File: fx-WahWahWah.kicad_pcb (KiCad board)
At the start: 2 copper layers, 58.4 x 76.2 mm, 37 parts, among them J1 Conn_01x10, Q1 2N5088, Q2 2N5089

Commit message: Fix readme, add OSHW silks
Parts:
- added QR*****: fx-WahWahWah-repo, QRCodes:fx-WahWahWah-repo, F.Cu at (96.1, 89.8)
- added REF**: OSHW-Symbol_8.9x8mm_SilkScreen, Symbol:OSHW-Symbol_8.9x8mm_SilkScreen, F.Cu at (96.1, 79.8)
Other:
- board text added: "CERN-OHL-P"

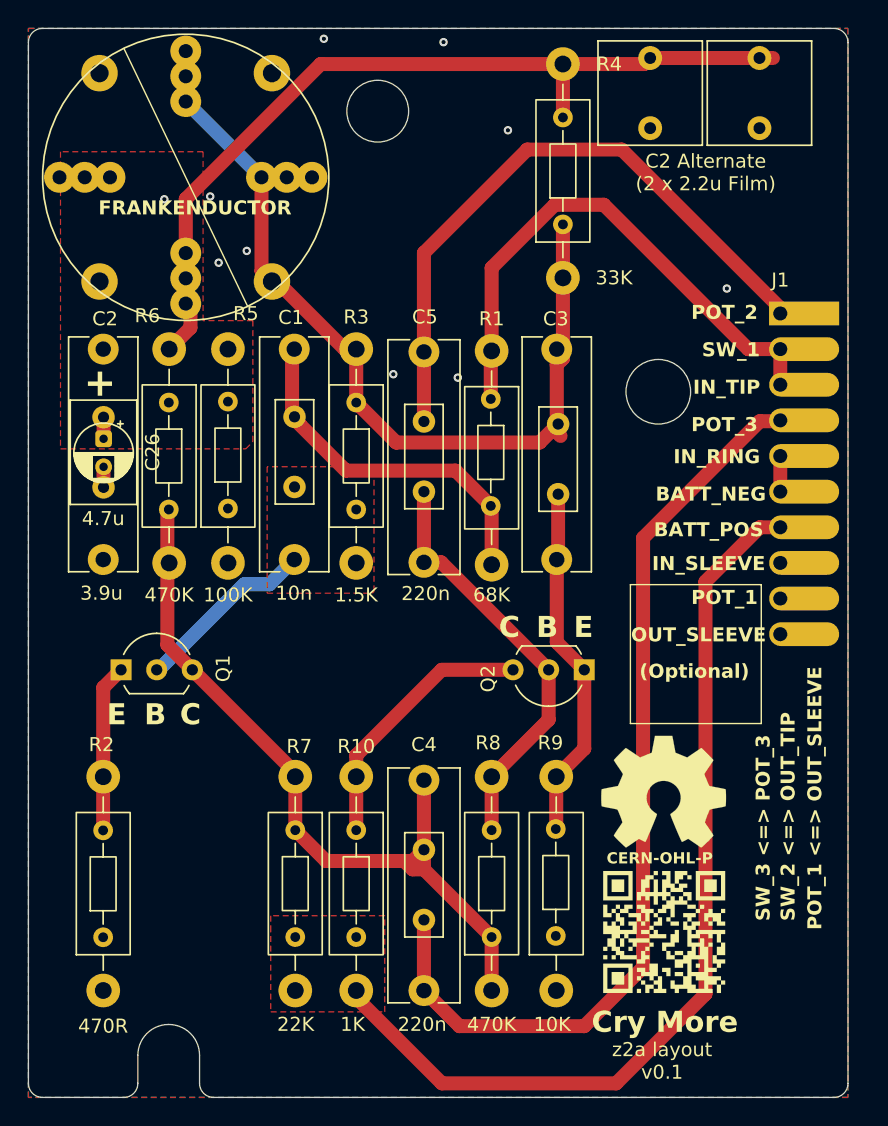
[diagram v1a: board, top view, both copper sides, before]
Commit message: Fix silks for OSHW/repo pointer
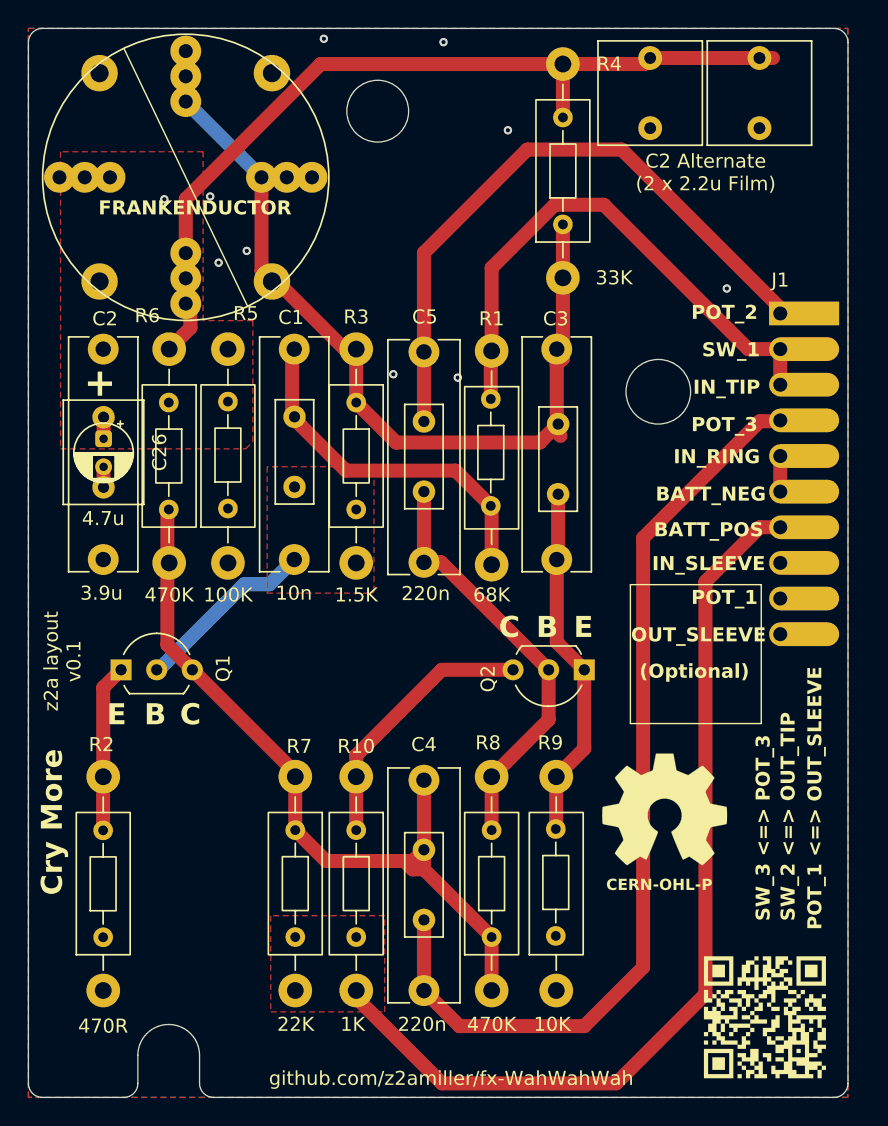
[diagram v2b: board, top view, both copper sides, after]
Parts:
- C26: footprint Capacitor_THT:C_Rect_L7.2mm_W4.5mm_P5.00mm_FKS2_FKP2_MKS2_MKP2 -> Capacitor_THT:C_Rect_L7.2mm_W5.5mm_P5.00mm_FKS2_FKP2_MKS2_MKP2
- moved QR***** 9.41 mm to (103.3, 95.9)
- moved REF** 1.26 mm to (96.1, 81.1)
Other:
- board text added: "github.com/z2amiller/fx-WahWahWah"
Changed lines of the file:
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@@
 			)
 		)
-		(attr through_hole)
+		(attr through_hole dnp)
 		(duplicate_pad_numbers_are_jumpers no)
 		(fp_line
@@
 			)
 		)
-		(attr through_hole)
+		(attr through_hole dnp)
 		(duplicate_pad_numbers_are_jumpers no)
 		(fp_line
@@
 			)
 		)
-		(attr through_hole)
+		(attr through_hole dnp)
 		(duplicate_pad_numbers_are_jumpers no)
 		(fp_line
@@
 			)
 		)
-		(attr through_hole)
+		(attr through_hole dnp)
 		(duplicate_pad_numbers_are_jumpers no)
 		(fp_line
@@
 			)
 		)
-		(attr through_hole)
+		(attr through_hole dnp)
 		(duplicate_pad_numbers_are_jumpers no)
 		(fp_line
@@
 			)
 		)
-		(attr through_hole)
+		(attr through_hole dnp)
 		(duplicate_pad_numbers_are_jumpers no)
 		(fp_line
@@
 			)
 		)
-		(attr through_hole)
+		(attr through_hole dnp)
 		(duplicate_pad_numbers_are_jumpers no)
 		(fp_line
@@
 		)
 	)
-	(footprint "Capacitor_THT:C_Rect_L7.2mm_W4.5mm_P5.00mm_FKS2_FKP2_MKS2_MKP2"
+	(footprint "Capacitor_THT:C_Rect_L7.2mm_W5.5mm_P5.00mm_FKS2_FKP2_MKS2_MKP2"
 		(layer "F.Cu")
 		(at 56.155 53.115 -90)
-		(descr "C, Rect series, Radial, pin pitch=5.00mm, length*width=7.2*4.5mm^2, Capacitor, http://www.wima.com/EN/WIMA_FKS_2.pdf")
-		(tags "C Rect series Radial pin pitch 5.00mm length 7.2mm width 4.5mm Capacitor")
+		(descr "C, Rect series, Radial, pin pitch=5.00mm, length*width=7.2*5.5mm^2, Capacitor, http://www.wima.com/EN/WIMA_FKS_2.pdf")
+		(tags "C Rect series Radial pin pitch 5.00mm length 7.2mm width 5.5mm Capacitor")
 		(property "Reference" "C26"
-			(at 2.5 -3.5 270)
+			(at 2.5 -4 270)
 			(layer "F.SilkS")
 			(effects
@@
 		)
 		(property "Value" "3.9u"
-			(at 2.5 3.5 270)
+			(at 2.5 4 270)
 			(layer "F.Fab")
 			(effects
@@
 		(sheetname "/")
 		(sheetfile "fx-WahWahWah.kicad_sch")
-		(attr through_hole)
+		(units
+			(unit
+				(name "A")
+				(pins "1" "2")
+			)
+		)
+		(attr through_hole dnp)
 		(duplicate_pad_numbers_are_jumpers no)
 		(fp_line
-			(start -1.22 2.37)
-			(end -1.22 -2.37)
+			(start -1.22 2.87)
+			(end -1.22 -2.87)
 			(stroke
 				(width 0.12)
@@
 		)
 		(fp_line
-			(start 6.22 2.37)
-			(end -1.22 2.37)
+			(start 6.22 2.87)
+			(end -1.22 2.87)
 			(stroke
 				(width 0.12)
@@
 		)
 		(fp_line
-			(start -1.22 -2.37)
-			(end 6.22 -2.37)
+			(start -1.22 -2.87)
+			(end 6.22 -2.87)
 			(stroke
 				(width 0.12)
@@
 		)
 		(fp_line
-			(start 6.22 -2.37)
-			(end 6.22 2.37)
+			(start 6.22 -2.87)
+			(end 6.22 2.87)
 			(stroke
 				(width 0.12)
@@
 		)
 		(fp_rect
-			(start -1.35 -2.5)
-			(end 6.35 2.5)
+			(start -1.35 -3)
+			(end 6.35 3)
 			(stroke
 				(width 0.05)
@@
 		)
 		(fp_rect
-			(start -1.1 -2.25)
-			(end 6.1 2.25)
+			(start -1.1 -2.75)
+			(end 6.1 2.75)
 			(stroke
 				(width 0.1)
@@
 		)
 		(embedded_fonts no)
-		(model "${KICAD10_3DMODEL_DIR}/Capacitor_THT.3dshapes/C_Rect_L7.2mm_W4.5mm_P5.00mm_FKS2_FKP2_MKS2_MKP2.step"
+		(model "${KICAD10_3DMODEL_DIR}/Capacitor_THT.3dshapes/C_Rect_L7.2mm_W5.5mm_P5.00mm_FKS2_FKP2_MKS2_MKP2.step"
 			(offset
 				(xyz 0 0 0)
@@
 			)
 		)
-		(attr through_hole)
+		(attr through_hole dnp)
 		(duplicate_pad_numbers_are_jumpers no)
 		(fp_line
@@
 			)
 		)
-		(attr through_hole)
+		(attr through_hole dnp)
 		(duplicate_pad_numbers_are_jumpers no)
 		(fp_line
@@
 	(footprint "QRCodes:fx-WahWahWah-repo"
 		(layer "F.Cu")
-		(at 96.12 89.81)
+		(at 103.3 95.89)
 		(property "Reference" "QR*****"
 			(at 0 5.65 0)
@@
 			)
 		)
+		(attr board_only)
 		(duplicate_pad_numbers_are_jumpers no)
 		(fp_rect
@@
 	(footprint "Symbol:OSHW-Symbol_8.9x8mm_SilkScreen"
 		(layer "F.Cu")
-		(at 96.067574 79.828677)
+		(at 96.14 81.09)
 		(descr "Open Source Hardware Symbol")
 		(tags "Logo Symbol OSHW")
@@
 			)
 		)
-		(attr exclude_from_pos_files exclude_from_bom allow_missing_courtyard)
+		(attr board_only exclude_from_pos_files exclude_from_bom allow_missing_courtyard)
 		(duplicate_pad_numbers_are_jumpers no)
 		(fp_poly
@@
 			)
 		)
-		(attr through_hole)
+		(attr through_hole dnp)
 		(duplicate_pad_numbers_are_jumpers no)
 		(fp_line
@@
 			)
 		)
-		(attr through_hole)
+		(attr through_hole dnp)
 		(duplicate_pad_numbers_are_jumpers no)
 		(fp_line
@@
 			)
 		)
-		(attr through_hole)
+		(attr through_hole dnp)
 		(duplicate_pad_numbers_are_jumpers no)
 		(fp_line
@@
 			)
 		)
-		(attr through_hole)
+		(attr through_hole dnp)
 		(duplicate_pad_numbers_are_jumpers no)
 		(fp_line
@@
 			)
 		)
-		(attr through_hole)
+		(attr through_hole dnp)
 		(duplicate_pad_numbers_are_jumpers no)
 		(fp_line
@@
 	)
 	(gr_text "CERN-OHL-P"
-		(at 92.01 85.02 0)
+		(at 91.98 86.91 0)
 		(layer "F.SilkS")
 		(effects
@@
 		)
 	)
+	(gr_text "github.com/z2amiller/fx-WahWahWah"
+		(at 67.94 100.83 0)
+		(layer "F.SilkS")
+		(effects
+			(font
+				(size 1 1)
+				(thickness 0.15)
+			)
+			(justify left bottom)
+		)
+	)
 	(gr_text "3.9u"
 		(at 56.007 65.659 0)
@@
 	)
 	(gr_text "z2a layout\nv0.1"
-		(at 95.97 100.39 0)
+		(at 54.63 70.51 90)
 		(layer "F.SilkS")
 		(effects
@@
 	)
 	(gr_text "Cry More"
-		(at 90.94 97.11 0)
+		(at 53.37 87.2 90)
 		(layer "F.SilkS")
 		(effects

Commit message: Some final silk cleanups
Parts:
- C26: footprint Capacitor_THT:C_Rect_L7.2mm_W5.5mm_P5.00mm_FKS2_FKP2_MKS2_MKP2 -> Capacitor_THT:C_Rect_L7.2mm_W4.5mm_P5.00mm_FKS2_FKP2_MKS2_MKP2
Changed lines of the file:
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@@
 		(tags "Resistor Axial_DIN0204 series Axial Horizontal pin pitch 7.62mm 0.167W length 3.6mm diameter 1.6mm")
 		(property "Reference" "R5"
-			(at 13.892585 1.278655 180)
+			(at 13.832585 0.068655 180)
 			(layer "F.SilkS")
 			(effects
@@
 		(tags "Resistor Axial_DIN0204 series Axial Horizontal pin pitch 7.62mm 0.167W length 3.6mm diameter 1.6mm")
 		(property "Reference" "R4"
-			(at 11.43 3.302 180)
+			(at 12.26 -3.35 180)
 			(layer "F.SilkS")
 			(effects
@@
 		)
 		(property "Value" "33K"
-			(at -3.81 3.645145 180)
+			(at -4.66 -3.68 180)
 			(layer "F.SilkS")
 			(effects
@@
 		)
 	)
-	(footprint "Capacitor_THT:C_Rect_L7.2mm_W5.5mm_P5.00mm_FKS2_FKP2_MKS2_MKP2"
+	(footprint "Capacitor_THT:C_Rect_L7.2mm_W4.5mm_P5.00mm_FKS2_FKP2_MKS2_MKP2"
 		(layer "F.Cu")
 		(at 56.155 53.115 -90)
-		(descr "C, Rect series, Radial, pin pitch=5.00mm, length*width=7.2*5.5mm^2, Capacitor, http://www.wima.com/EN/WIMA_FKS_2.pdf")
-		(tags "C Rect series Radial pin pitch 5.00mm length 7.2mm width 5.5mm Capacitor")
+		(descr "C, Rect series, Radial, pin pitch=5.00mm, length*width=7.2*4.5mm^2, Capacitor, http://www.wima.com/EN/WIMA_FKS_2.pdf")
+		(tags "C Rect series Radial pin pitch 5.00mm length 7.2mm width 4.5mm Capacitor")
 		(property "Reference" "C26"
-			(at 2.5 -4 270)
-			(layer "F.SilkS")
+			(at 2.5 -3.5 270)
+			(layer "F.SilkS")
+			(hide yes)
 			(effects
 				(font
@@
 		)
 		(property "Value" "3.9u"
-			(at 2.5 4 270)
+			(at 2.5 3.5 270)
 			(layer "F.Fab")
 			(effects
@@
 		(duplicate_pad_numbers_are_jumpers no)
 		(fp_line
-			(start -1.22 2.87)
-			(end -1.22 -2.87)
-			(stroke
-				(width 0.12)
-				(type solid)
-			)
-			(layer "F.SilkS")
-		)
-		(fp_line
-			(start 6.22 2.87)
-			(end -1.22 2.87)
-			(stroke
-				(width 0.12)
-				(type solid)
-			)
-			(layer "F.SilkS")
-		)
-		(fp_line
-			(start -1.22 -2.87)
-			(end 6.22 -2.87)
-			(stroke
-				(width 0.12)
-				(type solid)
-			)
-			(layer "F.SilkS")
-		)
-		(fp_line
-			(start 6.22 -2.87)
-			(end 6.22 2.87)
+			(start -1.22 2.37)
+			(end -1.22 -2.37)
+			(stroke
+				(width 0.12)
+				(type solid)
+			)
+			(layer "F.SilkS")
+		)
+		(fp_line
+			(start 6.22 2.37)
+			(end -1.22 2.37)
+			(stroke
+				(width 0.12)
+				(type solid)
+			)
+			(layer "F.SilkS")
+		)
+		(fp_line
+			(start -1.22 -2.37)
+			(end 6.22 -2.37)
+			(stroke
+				(width 0.12)
+				(type solid)
+			)
+			(layer "F.SilkS")
+		)
+		(fp_line
+			(start 6.22 -2.37)
+			(end 6.22 2.37)
 			(stroke
 				(width 0.12)
@@
 		)
 		(fp_rect
-			(start -1.35 -3)
-			(end 6.35 3)
+			(start -1.35 -2.5)
+			(end 6.35 2.5)
 			(stroke
 				(width 0.05)
@@
 		)
 		(fp_rect
-			(start -1.1 -2.75)
-			(end 6.1 2.75)
+			(start -1.1 -2.25)
+			(end 6.1 2.25)
 			(stroke
 				(width 0.1)
@@
 		)
 		(embedded_fonts no)
-		(model "${KICAD10_3DMODEL_DIR}/Capacitor_THT.3dshapes/C_Rect_L7.2mm_W5.5mm_P5.00mm_FKS2_FKP2_MKS2_MKP2.step"
+		(model "${KICAD10_3DMODEL_DIR}/Capacitor_THT.3dshapes/C_Rect_L7.2mm_W4.5mm_P5.00mm_FKS2_FKP2_MKS2_MKP2.step"
 			(offset
 				(xyz 0 0 0)

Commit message: fx-WahWahWah v0.1 fab outputs (g1)
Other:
- board text added: "z2a layout ${REVISION}"
- board text removed: "z2a layout v0.1"
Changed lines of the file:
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@@
 	)
 	(paper "A4")
+	(title_block
+		(rev "v0.1")
+	)
 	(layers
 		(0 "F.Cu" signal)
@@
 		)
 	)
-	(gr_text "z2a layout\nv0.1"
+	(gr_text "z2a layout\n${REVISION}"
 		(at 54.63 70.51 90)
 		(layer "F.SilkS")

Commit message: fx-WahWahWah v0.2 fab outputs (g2)
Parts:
- moved REF** 33.1 mm to (63.1, 83.2)
- moved J1 14.6 mm to (96.8, 58.2)
- moved QR***** 7.03 mm to (96.3, 95.9)
- moved C27 5.38 mm to (97.5, 27.7)
- moved C28 5.23 mm to (89.9, 27.7)
- moved R24 4.83 mm to (84.1, 43.2)
- moved R4 4.83 mm to (84.1, 39.4)
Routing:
- net POT_LUG_3: track 67.3 -> 50.7 mm
- net +9V: track 66.9 -> 50.8 mm
- net IN_JACK_TIP: track 38.6 -> 26.1 mm
- net POT_LUG_2: track 45.5 -> 56.2 mm
- net Net-(C2-Pad1): track 66.4 -> 61.1 mm
- net GND: track 1.46 -> 6.54 mm, vias 10 -> 36
- net Net-(C23-Pad2): track 59.8 -> 62.0 mm
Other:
- board size 58.4 x 76.2 mm -> 51.1 x 76.2 mm
- board text added: "BAT_N"
- board text added: "BAT_P"
- board text added: "IN_R"
- board text added: "IN_S"
- board text added: "OUT_S"
- board text removed: "BATT_NEG"
- board text removed: "BATT_POS"
- board text removed: "CERN-OHL-P"
- board text removed: "IN_RING"
- board text removed: "IN_SLEEVE"
- board text removed: "OUT_SLEEVE"

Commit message: fx-WahWahWah v0.3 fab outputs (g3)
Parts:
- removed J1: Conn_01x10, Connector_PinHeader_2.54mm:PinHeader_1x10_P2.54mm_Vertical
- added J10: Conn_01x01_Pin, TestPoint:Vector T46-5-9M, F.Cu at (94.0, 86.4)
- added J11: Conn_01x01_Pin, TestPoint:Vector T46-5-9M, F.Cu at (99.1, 88.9)
- added J2: Conn_01x01_Pin, TestPoint:Vector T46-5-9M, F.Cu at (99.1, 38.1)
- added J3: Conn_01x01_Pin, TestPoint:Vector T46-5-9M, F.Cu at (94.0, 43.2)
- added J4: Conn_01x01_Pin, TestPoint:Vector T46-5-9M, F.Cu at (99.1, 45.7)
- added J5: Conn_01x01_Pin, TestPoint:Vector T46-5-9M, F.Cu at (99.1, 66.0)
- added J6: Conn_01x01_Pin, TestPoint:Vector T46-5-9M, F.Cu at (99.1, 73.7)
- added J7: Conn_01x01_Pin, TestPoint:Vector T46-5-9M, F.Cu at (94.0, 71.1)
- added J8: Conn_01x01_Pin, TestPoint:Vector T46-5-9M, F.Cu at (94.0, 78.7)
- added J9: Conn_01x01_Pin, TestPoint:Vector T46-5-9M, F.Cu at (99.1, 83.8)
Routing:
- net POT_LUG_2: track 56.2 -> 35.9 mm
- net +9V: track 50.8 -> 56.7 mm
- net GND: track 6.54 -> 1.46 mm, vias 36 -> 33
- net IN_JACK_TIP: track 26.1 -> 21.9 mm
- net BATT_NEG: track 2.54 -> 6.13 mm
- net POT_LUG_3: track 50.7 -> 51.9 mm
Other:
- board text added: "(Wire Wrap) Vector T46-5-9"
- board text added: "2 x 2.2u Film"
- board text added: "C2 Alternate"
- board text removed: "(Optional)"
- board text removed: "C2 Alternate (2 x 2.2u Film)"
